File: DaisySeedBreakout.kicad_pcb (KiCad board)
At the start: 2 copper layers, 56.1 x 65 mm, 194 parts, among them J1 Conn_01x03, J10 Conn_01x02, J11 Conn_01x02, J12 Conn_01x02, J13 Conn_01x02, J14 Conn_01x02, J15 Conn_01x03, J16 Conn_02x04, J2 Conn_01x02, J20 Conn_01x02, J21 Conn_01x02, J22 Conn_01x02, J24 Conn_01x02, J25 Conn_01x02, J27 Conn_01x03, J3 Conn_01x03, J30 Conn_01x02, J31 Conn_02x04, J35 Conn_01x02, J4 5027740891, J47 Conn_01x03, J48 Conn_01x03, J49 Conn_01x03, J50 Conn_01x03, J51 Conn_01x03, J52 Conn_01x03, J53 Conn_01x03, J54 Conn_01x03, J55 Conn_01x03, J56 Conn_01x03, J57 Conn_01x03, J58 Conn_01x03, J59 Conn_01x03, J6 Conn_01x02, J60 Conn_01x03, J61 Conn_01x03, J62 Conn_01x03, J63 Conn_01x03, J64 Conn_01x03, J65 Conn_01x03, J67 Conn_01x02, J68 Conn_01x02, J69 Conn_01x02, J70 Conn_01x02, J8 Conn_01x02, J9 Conn_01x02, U1 H11L1M, U10 TPD2EUSB30ADRTR, U2 PAM8320RDR, U4 ATMEGA1608-MFR, U5 MAX9814, U6 DSC6001CE2A-010.0000, U7 TLV9062IDR

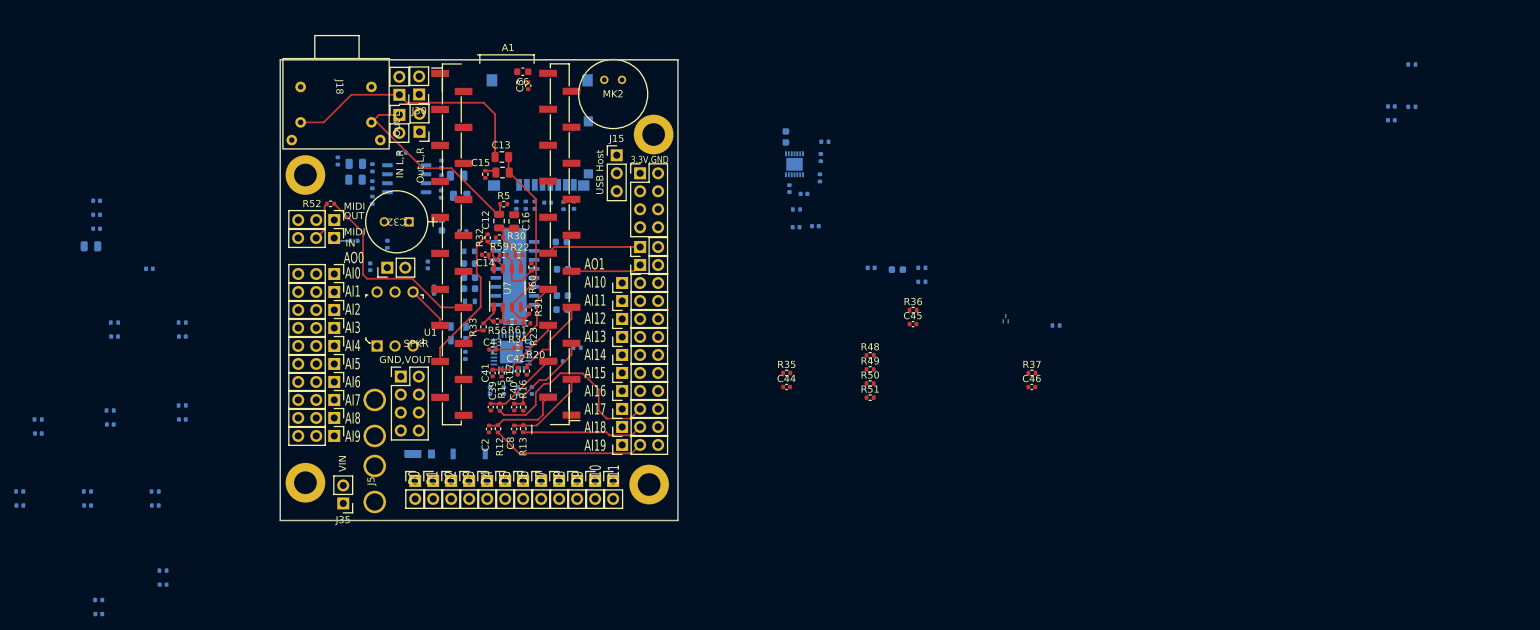
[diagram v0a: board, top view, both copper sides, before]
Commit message: simplified design, rely on external boards more to cover those cases
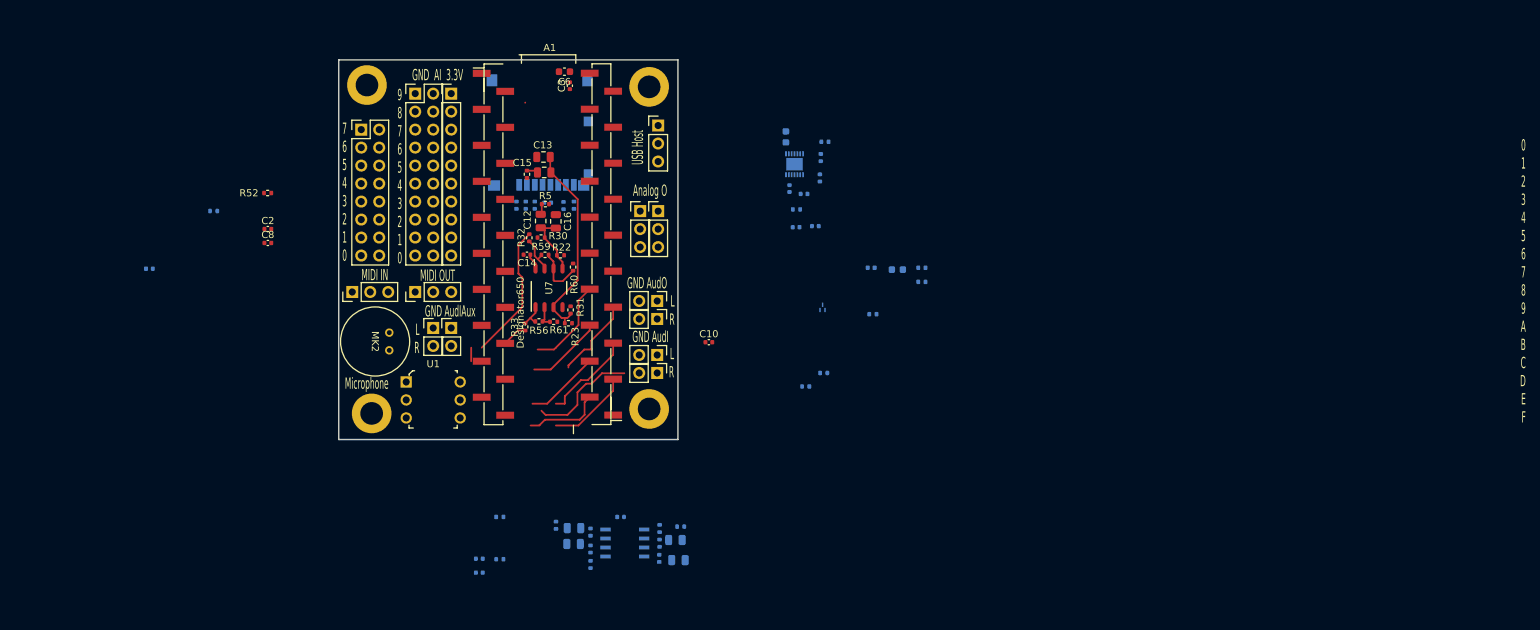
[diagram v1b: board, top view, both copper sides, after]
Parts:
- removed C25: 220pF, Capacitor_SMD:C_0402_1005Metric
- removed C26, C27, C28, C29, C30: 1u, Capacitor_SMD:C_0603_1608Metric
- removed C31, C36, C37, C38, C57, C58, C59: 0.1uF, Capacitor_SMD:C_0402_1005Metric
- removed C32: 860020474014, 470uF:CAP_WCAP-ATG5_8x11.5_WRE
- removed C33, C34, C35: 0.1uF, Capacitor_SMD:C_0603_1608Metric
- removed C39, C40, C41, C42, C43, C44, C45, C46, C47, C48, C49, C50, C51, C52, C53, C54, C55, C56: SPARE, Capacitor_SMD:C_0402_1005Metric
- removed C60: 47uF, Capacitor_SMD:C_0805_2012Metric
- removed CR1: DFLT15A-7, TVSDiode:ZDO_POWERDI123_DIO
- removed FB1, FB2: MPZ1608S221ATA00, digikey-footprints:0603
- removed J16, J31: Conn_02x04, Connector_PinHeader_2.54mm:PinHeader_2x04_P2.54mm_Vertical
- removed J18: ~, Ultralibrarian:STX-4235-3-3-N
- removed J20, J21, J22, J24, J25, J30, J35, J67, J68, J69, J70: Conn_01x02, Connector_PinHeader_2.54mm:PinHeader_1x02_P2.54mm_Vertical
- removed J27, J47, J48, J49, J50, J51, J52, J53, J54, J55, J56, J57, J58, J59, J60, J61, J62, J63, J64, J65: Conn_01x03, Ultralibrarian:PinHeader_1x03_P2.54mm_Vertical_Female
- removed R12, R13, R15, R16, R17, R20, R34, R35, R36, R37, R38, R39, R40, R41, R42, R43, R44, R45, R46, R47: 1k, Resistor_SMD:R_0402_1005Metric
- removed R48, R49, R50, R51: 10k, Resistor_SMD:R_0402_1005Metric
- removed R57, R58: 4.7k, Resistor_SMD:R_0402_1005Metric
- removed R65: 0, Resistor_SMD:R_0402_1005Metric
- removed R95: 33.2, Resistor_SMD:R_0402_1005Metric
- removed U2: PAM8320RDR, PAM8320:SO-16EP_3P9X9P9_DIO
- removed U4: ATMEGA1608-MFR, atmega:VQFN32_RXB_MCH-M
- removed U6: DSC6001CE2A-010.0000, oscillator:DFN4_3.2X2.5_MCH
- removed Z56: RSX501LAM20TR, 5ADiode:DIO_RB050LAM_ROM
- added J7: Conn_01x10, Connector_PinHeader_2.54mm:PinHeader_1x10_P2.54mm_Vertical, F.Cu at (132.1, 36.8)
- C10: value 220pF -> 0.1uF; moved to F.Cu
- C2, C8: value SPARE -> 0.1uF
- J10, J14: value Conn_01x02 -> Conn_01x03; footprint Connector_PinHeader_2.54mm:PinHeader_1x02_P2.54mm_Vertical -> Ultralibrarian:PinHeader_1x03_P2.54mm_Vertical_Female
- J11, J12, J13, J2, J8, J9: footprint Connector_PinHeader_2.54mm:PinHeader_1x02_P2.54mm_Vertical -> 1x2FemaleVertical:PinHeader_1x02_P2.54mm_VerticalFemale
- J5: value ~ -> Conn_02x08; footprint Ultralibrarian:BladeFuseHolder -> Connector_PinHeader_2.54mm:PinHeader_2x08_P2.54mm_Vertical
- J6: value Conn_01x02 -> Pins_02x10_P2.54mm_TH; footprint Connector_PinHeader_2.54mm:PinHeader_1x02_P2.54mm_Vertical -> Connector_PinHeader_2.54mm:PinHeader_2x10_P2.54mm_Vertical
- moved C70 143.7 mm to (136.1, 102.4)
- moved C71 143.7 mm to (136.1, 104.4)
- moved R66 143.7 mm to (138.9, 102.5)
- moved R8 143.7 mm to (138.9, 96.5)
- moved C5 59.9 mm to (149.4, 100.3)
- moved R10 59.9 mm to (161.4, 102.4)
- moved R19 59.9 mm to (151.7, 98.7)
- moved R67 59.9 mm to (151.7, 103.2)
- moved U3 59.9 mm to (156.6, 100.2)
- moved C11 59.9 mm to (163.7, 99.8)
- moved C17 59.9 mm to (149.4, 98.1)
- moved C4 59.9 mm to (164.2, 102.6)
- moved R18 59.9 mm to (161.5, 98.2)
- moved R24 59.9 mm to (164.5, 97.9)
- moved R25 59.9 mm to (146.9, 97.7)
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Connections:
- A1 pad 10: /arduino_coprocessor/UART0_RXD_SPI0_MISO -> /DIO6
- A1 pad 11: /arduino_coprocessor/UART0_TXD_SPI0_MOSI -> /DIO7
- A1 pad 12: /GPIO_Conn11/GPIO_Conn -> /DIO2
- A1 pad 13: /GPIO_Conn12/GPIO_Conn -> /DIO3
- A1 pad 22: /AI0 -> /AI_0
- A1 pad 23: /AI1 -> /AI_1
- A1 pad 24: /AI2 -> /AI_2
- A1 pad 25: /AI3 -> /AI_3
- A1 pad 26: /AI4 -> /AI_4
- A1 pad 27: /AI5 -> /AI_5
- A1 pad 28: /AI6 -> /AI_6
- A1 pad 29: /AO0 -> /AO_0
- A1 pad 30: /AO1 -> /AO_1
- A1 pad 31: /AI9 -> /AI_7
- A1 pad 32: /AI10 -> /AI_8
- A1 pad 33: /RESET_n -> /DIO0
- A1 pad 34: /UPDI -> /DIO1
- A1 pad 35: /AI11 -> /AI_9
- A1 pad 8: /arduino_coprocessor/SPI0_CS -> /DIO4
- A1 pad 9: /arduino_coprocessor/SPI0_SCLK -> /DIO5
- C10 pad 1: /ClassD_20W_Amp/OUT_N -> +3.3VA
- C2 pad 1: /AI0 -> +3.3VA
- C8 pad 1: /AI1 -> +3.3VA
- J1 pad 1: Net-(J1-Pin_1) -> GND
- J1 pad 3: GND -> Net-(J1-Pin_3)
- J10 pad 1: /GPIO_Conn3/GPIO_Conn -> GND
- J10 pad 2: GND -> /AO_0
- J11 pad 1: /GPIO_Conn/GPIO_Conn -> /Audio Out/AUDIO_OUT_R_EXT
- J12 pad 1: /GPIO_Conn7/GPIO_Conn -> /Audio In Sum/AUDIO_IN_L_CONN
- J13 pad 1: /GPIO_Conn4/GPIO_Conn -> /Audio In Sum/AUDIO_IN_R_CONN
- J14 pad 1: /GPIO_Conn5/GPIO_Conn -> GND
- J14 pad 2: GND -> /AO_1
- J2 pad 1: /ClassD_20W_Amp/OUT_P -> /Audio Out/AUDIO_OUT_L_EXT
- J2 pad 2: /ClassD_20W_Amp/OUT_N -> GND
- J3 pad 1: Net-(J3-Pin_1) -> GND
- J3 pad 3: GND -> Net-(J3-Pin_3)
- J5 pad 1: Net-(J35-Pin_1) -> GND
- J5 pad 2: Net-(J35-Pin_1) -> /DIO0
- J5 pad 3: Net-(J16-Pin_2) -> GND
- J5 pad 4: Net-(J16-Pin_2) -> /DIO1
- J6 pad 1: /Audio Out/AUDIO_OUT_L_EXT -> GND
- J6 pad 2: GND -> /AI_0
- J8 pad 1: /GPIO_Conn1/GPIO_Conn -> unconnected-(J8-Pin_1-Pad1)
- J9 pad 1: /GPIO_Conn2/GPIO_Conn -> unconnected-(J9-Pin_1-Pad1)
- R11 pad 2: /GPIO_Conn11/GPIO_Conn -> /DIO2
- R53 pad 2: Net-(J1-Pin_1) -> Net-(J1-Pin_3)
- R54 pad 2: Net-(J3-Pin_1) -> Net-(J3-Pin_3)
- R6 pad 2: /GPIO_Conn12/GPIO_Conn -> /DIO3
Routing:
- net /Audio In Sum/AUDIO_IN_L_CONN: track 37.8 -> 1.53 mm
- net Net-(J48-Pin_2): track 28.5 -> 0.00 mm
- net /MIDI_UART_TX: track 27.8 -> 0.00 mm
- net /Audio In Sum/AUDIO_IN_R_CONN: track 29.3 -> 1.73 mm
- net Net-(J27-Pin_2): track 21.8 -> 0.00 mm
- net Net-(J47-Pin_2): track 17.3 -> 0.00 mm
- net (no net): track 0.00 -> 15.4 mm
- net /AO1: track 13.4 -> 0.00 mm
- net /AI3: track 13.2 -> 0.00 mm
- net /AI_3: track 0.00 -> 13.2 mm
- net /AI6: track 12.9 -> 0.00 mm
- net /AI_6: track 0.00 -> 12.9 mm
- net /AI5: track 11.8 -> 0.00 mm
- net /AI_5: track 0.00 -> 11.8 mm
- net /AI1: track 11.8 -> 0.00 mm
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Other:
- board size 56.1 x 65 mm -> 47.9 x 53.6 mm
- board text added: "0 1 2 3 4 5 6 7 8 9 A B C D E F"
- board text added: "7 6 5 4 3 2 1 0"
- board text added: "9 8 7 6 5 4 3 2 1 0"
- board text added: "Analog O"
- board text added: "GND AI 3.3V"
- board text added: "GND AudI"
- board text added: "GND AudIAux"
- board text added: "GND AudO"
- board text added: "L R"
- board text added: "MIDI IN"
- board text added: "MIDI OUT"
- board text added: "Microphone"
- board text removed: "3.3V,GND"
- board text removed: "AI0 AI1 AI2 AI3 AI4 AI5 AI6 AI7 AI8 AI9"
- board text removed: "AO0"
- board text removed: "AO1 AI10 AI11 AI12 AI13 AI14 AI15 AI16 AI17 AI18 AI19"
- board text removed: "D0 D1 D2 D3 D4 D5 D6 D7 D8 D9 D10 D11"
- board text removed: "GND,VOUT"
- board text removed: "IN"
- board text removed: "IN L,R"
- board text removed: "MIDI"
- board text removed: "OUT"
- board text removed: "Out L"
- board text removed: "Out L,R"
- board text removed: "SPKR"
- board text removed: "VIN"

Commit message: started layout
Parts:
- added J16: Conn_01x02, 1x2FemaleVertical:PinHeader_1x02_P2.54mm_VerticalFemale, F.Cu at (163.8, 88.9)
- A1: footprint Module:Electrosmith_Daisy_Seed -> ElectgrosmithSurfaceMountModule:Electrosmith_Daisy_Seed
- C11, C17, C24, C4, C5, C70, C71, C9, D1, R10, R11, R18, R19, R24, R25, R53, R54, R55, R6, R62, R66, R67, R7, R8, R9, U10, U3: moved to F.Cu
- C6: footprint Capacitor_SMD:C_0603_1608Metric -> Capacitor_SMD:C_0402_1005Metric
- C7: footprint Capacitor_SMD:C_0603_1608Metric -> Capacitor_SMD:C_0402_1005Metric; moved to F.Cu
- moved R54 68.4 mm to (131.1, 72.9), turned to 90 degrees
- moved C7 67.9 mm to (128.1, 72.9), turned to -90 degrees
- moved R55 66.2 mm to (133.0, 72.9), turned to -90 degrees
- moved C9 63.4 mm to (149.4, 82.2)
- moved D1 62.7 mm to (129.8, 72.9), turned to 90 degrees
- moved R62 59.7 mm to (142.3, 34.3), turned to -90 degrees
- moved R26 53.2 mm to (137.6, 71.6), turned to 0 degrees
- moved R11 51.5 mm to (135.0, 62.7), turned to 180 degrees
- moved C20 50.1 mm to (143.8, 78.2), turned to 90 degrees
- moved R27 49.9 mm to (145.0, 73.6), turned to -90 degrees
- moved C18 49.4 mm to (137.7, 73.0)
- moved R6 49.1 mm to (134.5, 65.9), turned to 90 degrees
- moved U5 46.9 mm to (142.6, 74.3), turned to 90 degrees
- moved R29 46.4 mm to (140.1, 75.4), turned to -90 degrees
- moved C22 46.4 mm to (142.1, 77.2), turned to 0 degrees
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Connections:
- A1 pad 10: /DIO6 -> /DIO4
- A1 pad 11: /DIO7 -> /DIO5
- A1 pad 12: /DIO2 -> /DIO0
- A1 pad 13: /DIO3 -> /DIO1
- A1 pad 33: /DIO0 -> /DIO6
- A1 pad 34: /DIO1 -> /DIO7
- A1 pad 39: +12V -> unconnected-(A1-VIN-Pad39)
- A1 pad 8: /DIO4 -> /DIO2
- A1 pad 9: /DIO5 -> /DIO3
- C16 pad 1: GND -> /Audio In Sum/AUDIO_IN_R_LOCAL
- C6 pad 1: +12V -> +3.3VA
- J8 pad 1: unconnected-(J8-Pin_1-Pad1) -> +3.3VA
- J9 pad 1: unconnected-(J9-Pin_1-Pad1) -> /Audio In Sum/AUDIO_IN_R_LOCAL
- R11 pad 2: /DIO2 -> /DIO0
- R6 pad 2: /DIO3 -> /DIO1
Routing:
- net GND: track 0.00 -> 57.9 mm, vias 0 -> 30
- net /microSD/D3: track 0.00 -> 29.1 mm, vias 0 -> 1
- net +3.3V: track 0.00 -> 26.1 mm, vias 0 -> 6
- net /microSD/D2: track 0.00 -> 23.5 mm, vias 0 -> 1
- net /Audio In Sum/AUDIO_IN_R_SUMMED: track 21.2 -> 0.00 mm
- net Net-(D1-A): track 0.00 -> 20.0 mm
- net Net-(U7A-IN+): track 29.2 -> 9.38 mm
- net +3.3VA: track 2.26 -> 21.0 mm, vias 0 -> 1
- net /microSD/D0: track 0.00 -> 18.1 mm, vias 0 -> 1
- net /microSD/D1: track 0.00 -> 17.9 mm, vias 0 -> 1
- net /MIDI_UART_RX: track 0.00 -> 15.9 mm
- net Net-(MK2-+): track 0.00 -> 15.9 mm
- net /microSD/CLK: track 0.00 -> 15.5 mm, vias 0 -> 1
- net (no net): track 15.4 -> 0.00 mm
- net /microSD/CMD: track 0.00 -> 15.3 mm, vias 0 -> 1
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- added copper zone on F.Cu, net +3.3VA
- added copper zone on In1.Cu, net GND
- added copper zone on In2.Cu, net GND
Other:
- copper layers 2 -> 4
- board text added: "GND AO 3.3V"
- board text added: "GND DIO"
- board text added: "R"

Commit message: partially routed
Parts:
- removed C18: 0.1uF, Capacitor_SMD:C_0402_1005Metric
- removed C19: 0.47uF, Capacitor_SMD:C_0402_1005Metric
- removed C20: 2.2uF, Capacitor_SMD:C_0603_1608Metric
- removed C21: 470nF, Capacitor_SMD:C_0402_1005Metric
- removed C22: 1uF, Capacitor_SMD:C_0402_1005Metric
- removed J8: Conn_01x02, 1x2FemaleVertical:PinHeader_1x02_P2.54mm_VerticalFemale
- removed MK2: Microphone_Condenser, microphone:MIC_AOM-6545_PUI
- removed R26: 2.21k, Resistor_SMD:R_0402_1005Metric
- removed R27, R28: 150k, Resistor_SMD:R_0402_1005Metric
- removed U5: MAX9814, Package_DFN_QFN:DFN-14-1EP_3x3mm_P0.4mm_EP1.78x2.35mm
- added C23: 0.1uF, Capacitor_SMD:C_0402_1005Metric, B.Cu at (148.4, 83.3)
- added C25: 0.1uF, Capacitor_SMD:C_0402_1005Metric, B.Cu at (144.3, 78.8)
- added C26: 0.01uF, Capacitor_SMD:C_0402_1005Metric, B.Cu at (143.7, 82.2)
- added C27: 100pF, Capacitor_SMD:C_0402_1005Metric, B.Cu at (148.3, 78.2)
- added C28: 1uF, Capacitor_SMD:C_0603_1608Metric, B.Cu at (147.7, 75.5)
- added J17: Conn_01x02, 1x2FemaleVertical:PinHeader_1x02_P2.54mm_VerticalFemale, F.Cu at (120.0, 76.9)
- added R12: 2k, Resistor_SMD:R_0402_1005Metric, B.Cu at (143.3, 77.7)
- added R13: 2k, Resistor_SMD:R_0402_1005Metric, B.Cu at (143.3, 79.8)
- added R15: 1M, Resistor_SMD:R_0402_1005Metric, B.Cu at (145.2, 83.3)
- added R16: 1M, Resistor_SMD:R_0402_1005Metric, B.Cu at (145.2, 81.2)
- added R17: 100k, Resistor_SMD:R_0402_1005Metric, B.Cu at (148.3, 77.0)
- added R20: 10k, Resistor_SMD:R_0402_1005Metric, B.Cu at (146.8, 77.2)
- added U2: MAX4466EXK_T, digikey-footprints:SOT-353, B.Cu at (148.3, 80.8)
- C11, C12, C17, C24, C4, C5, C70, C71, R10, R18, R19, R24, R25, R5, R66, R67, R7, R8, R9, U3: moved to B.Cu
- moved J16 47.6 mm to (120.3, 69.5), turned to 90 degrees
- moved C11 39.3 mm to (153.7, 64.8), turned to 0 degrees
- moved R24 39.2 mm to (154.9, 63.2)
- moved C17 35.8 mm to (142.2, 65.5)
- moved R25 35.7 mm to (144.8, 65.3), turned to 90 degrees
- moved C71 34.6 mm to (140.2, 69.8), turned to 180 degrees
- moved R18 34.2 mm to (152.1, 66.3), turned to 180 degrees
- moved R8 34.1 mm to (152.4, 68.1), turned to 90 degrees
- moved C5 33.4 mm to (140.0, 71.6), turned to 0 degrees
- moved R19 33.1 mm to (142.2, 67.6)
- moved R66 32.1 mm to (142.3, 69.5)
- moved R67 31.5 mm to (145.0, 72.9), turned to 0 degrees
- moved U3 30.9 mm to (147.3, 69.3), turned to 180 degrees
- moved C24 30.7 mm to (146.3, 65.8), turned to 0 degrees
- moved R9 30.1 mm to (143.0, 72.9), turned to 0 degrees
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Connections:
- C24 pad 1: /Audio Out/VCC -> +3.3VA
- J16 pad 1: +3.3V -> GND
- J16 pad 2: GND -> +3.3V
- J5 pad 10: /DIO4 -> /DIO3
- J5 pad 12: /DIO5 -> /DIO2
- J5 pad 14: /DIO6 -> /DIO1
- J5 pad 16: /DIO7 -> /DIO0
- J5 pad 2: /DIO0 -> /DIO7
- J5 pad 4: /DIO1 -> /DIO6
- J5 pad 6: /DIO2 -> /DIO5
- J5 pad 8: /DIO3 -> /DIO4
- J6 pad 10: /AI_4 -> /AI_5
- J6 pad 12: /AI_5 -> /AI_4
- J6 pad 14: /AI_6 -> /AI_3
- J6 pad 16: /AI_7 -> /AI_2
- J6 pad 18: /AI_8 -> /AI_1
- J6 pad 2: /AI_0 -> /AI_9
- J6 pad 20: /AI_9 -> /AI_0
- J6 pad 4: /AI_1 -> /AI_8
- J6 pad 6: /AI_2 -> /AI_7
- J6 pad 8: /AI_3 -> /AI_6
- R7 pad 1: /Audio Out/VCC -> +3.3VA
- R9 pad 1: /Audio Out/VCC -> +3.3VA
- U3 pad 8: /Audio Out/VCC -> +3.3VA
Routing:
- net /DIO6: track 0.00 -> 49.9 mm
- net /DIO7: track 0.00 -> 45.8 mm
- net /AI_0: track 0.00 -> 43.4 mm, vias 0 -> 1
- net /AI_1: track 0.00 -> 40.4 mm, vias 0 -> 1
- net /AI_6: track 0.00 -> 40.2 mm, vias 0 -> 1
- net /AI_3: track 0.00 -> 38.1 mm, vias 0 -> 1
- net /AI_7: track 0.00 -> 37.1 mm, vias 0 -> 1
- net /AI_5: track 0.00 -> 36.6 mm, vias 0 -> 1
- net /AI_8: track 0.00 -> 34.6 mm, vias 0 -> 1
- net /AI_4: track 0.00 -> 34.0 mm, vias 0 -> 1
- net /DIO5: track 0.00 -> 33.7 mm
- net /DIO2: track 0.00 -> 33.1 mm
- net /AI_9: track 0.00 -> 29.6 mm, vias 0 -> 1
- net Net-(J17-Pin_1): track 0.00 -> 29.1 mm
- net /MIDI_UART_TX: track 0.00 -> 26.6 mm, vias 0 -> 2
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- added copper zone on F.Cu, net +3.3V
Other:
- board text added: "GND AI 3.3VA"
- board text added: "GND, 3.3VD"
- board text removed: "GND AI 3.3V"

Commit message: partially routed
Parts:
- moved R53 10.8 mm to (125.5, 67.1)
- moved R52 0.51 mm to (125.7, 68.8)
- moved R20 0.25 mm to (146.8, 77.5)
- moved C28 0.22 mm to (147.7, 75.7)
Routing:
- net +3.3V: track 51.8 -> 195.5 mm, vias 6 -> 7
- net +3.3VA: track 25.7 -> 101.7 mm, vias 5 -> 11
- net /AI_2: track 10.7 -> 42.5 mm, vias 0 -> 1
- net Net-(U7B-IN+): track 7.21 -> 30.9 mm, vias 0 -> 1
- net /Audio In Sum/AUDIO_IN_R_SUMMED: track 0.00 -> 23.1 mm
- net /Audio In Sum/AUDIO_IN_L_CONN: track 0.00 -> 14.6 mm
- net /Audio In Sum/AUDIO_IN_L_LOCAL: track 0.00 -> 11.5 mm, vias 0 -> 1
- net /Audio Out/AUDIO_OUT_R: track 0.00 -> 9.18 mm, vias 0 -> 1
- net /AI_6: track 40.2 -> 33.6 mm
- net /Audio Out/AUDIO_OUT_R_EXT: track 24.5 -> 29.6 mm
- net /MIDI_UART_TX: track 26.6 -> 22.2 mm
- net /Audio In Sum/AUDIO_IN_L_SUMMED: track 0.00 -> 3.51 mm
- net Net-(J1-Pin_3): track 0.00 -> 3.02 mm
- net Net-(R18-Pad1): track 1.37 -> 3.85 mm
- net GND: track 78.8 -> 80.5 mm, vias 43 -> 44
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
